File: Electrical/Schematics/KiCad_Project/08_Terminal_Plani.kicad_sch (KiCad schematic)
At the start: 0 parts

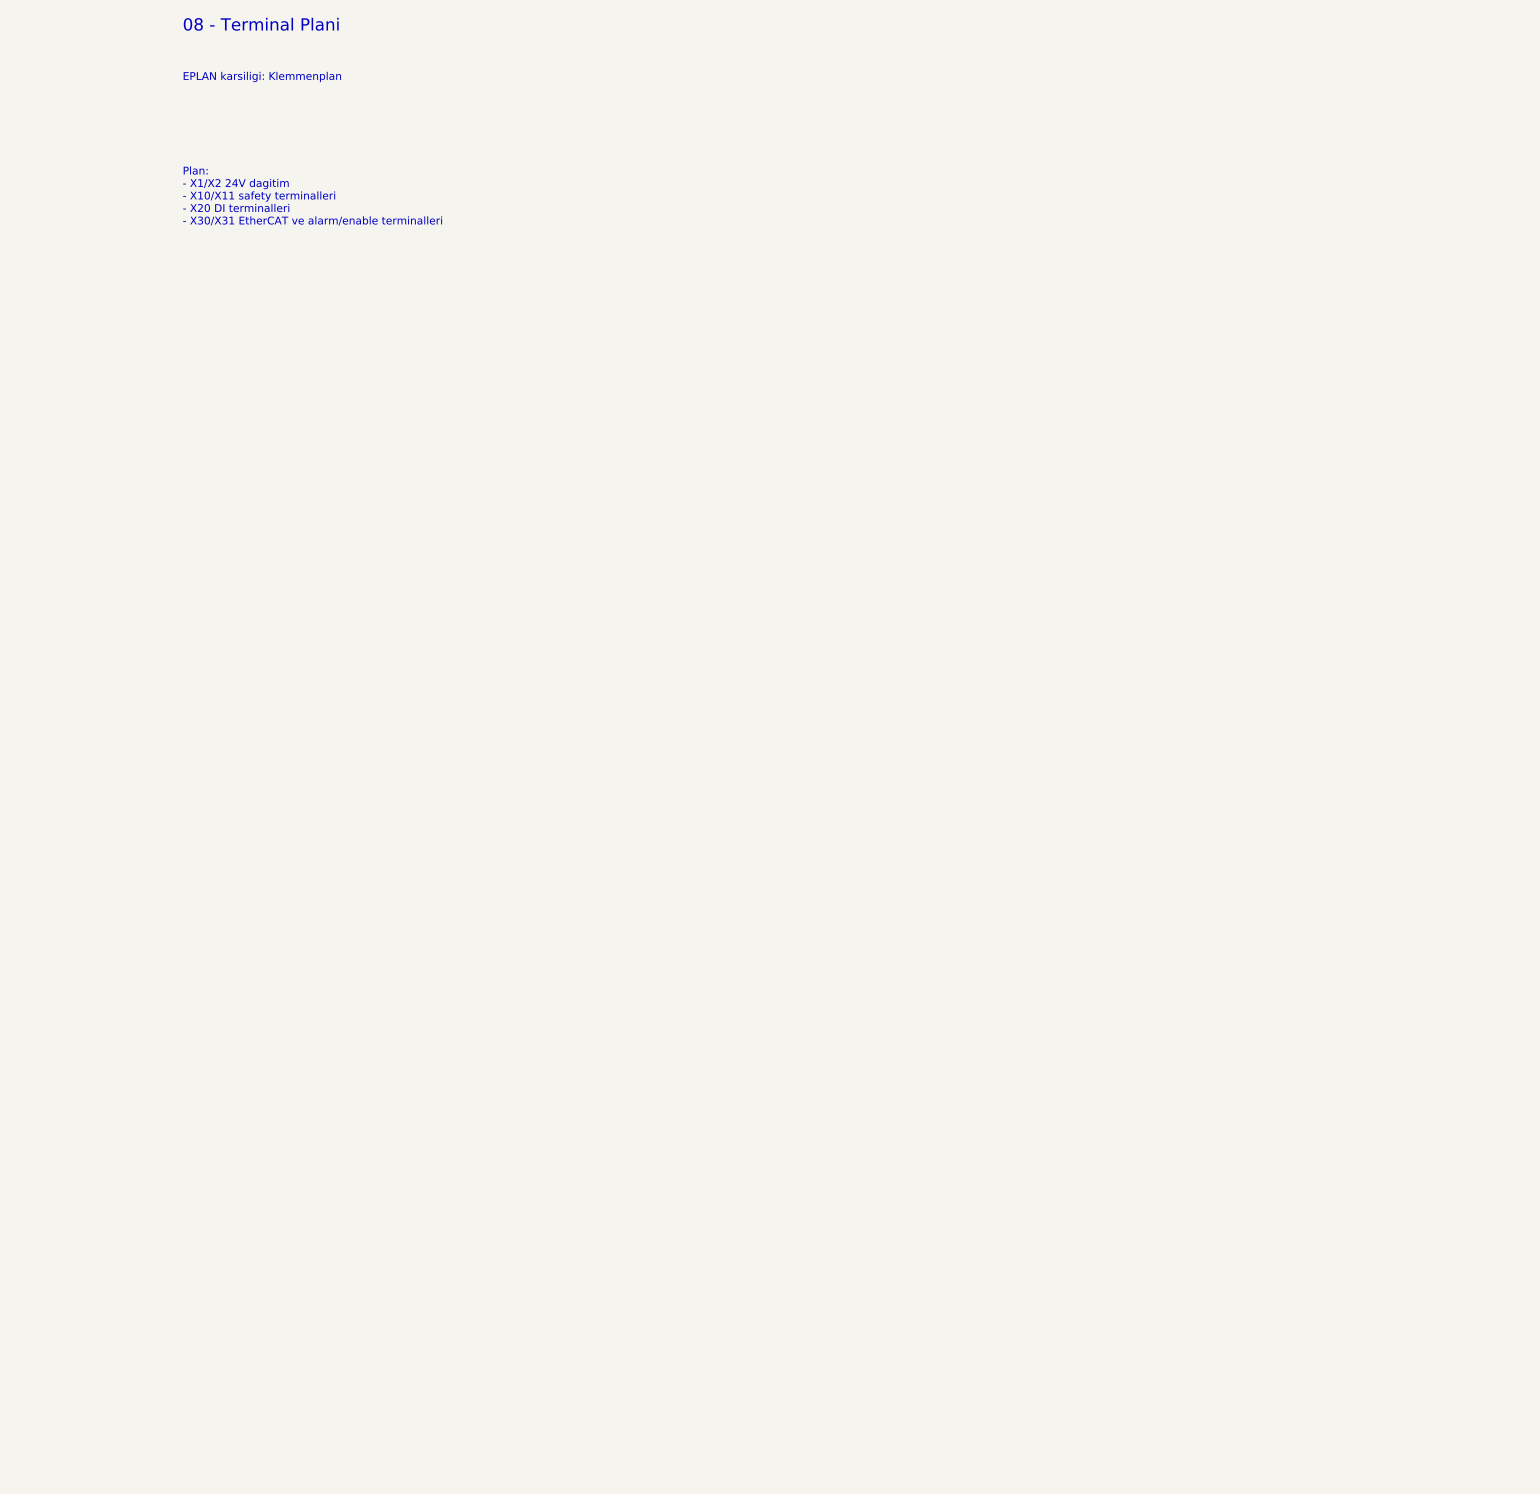
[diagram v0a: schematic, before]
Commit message: feat: update electrical schematics to rev 4.0, add technical manuals, and include project documentation and validation reports.
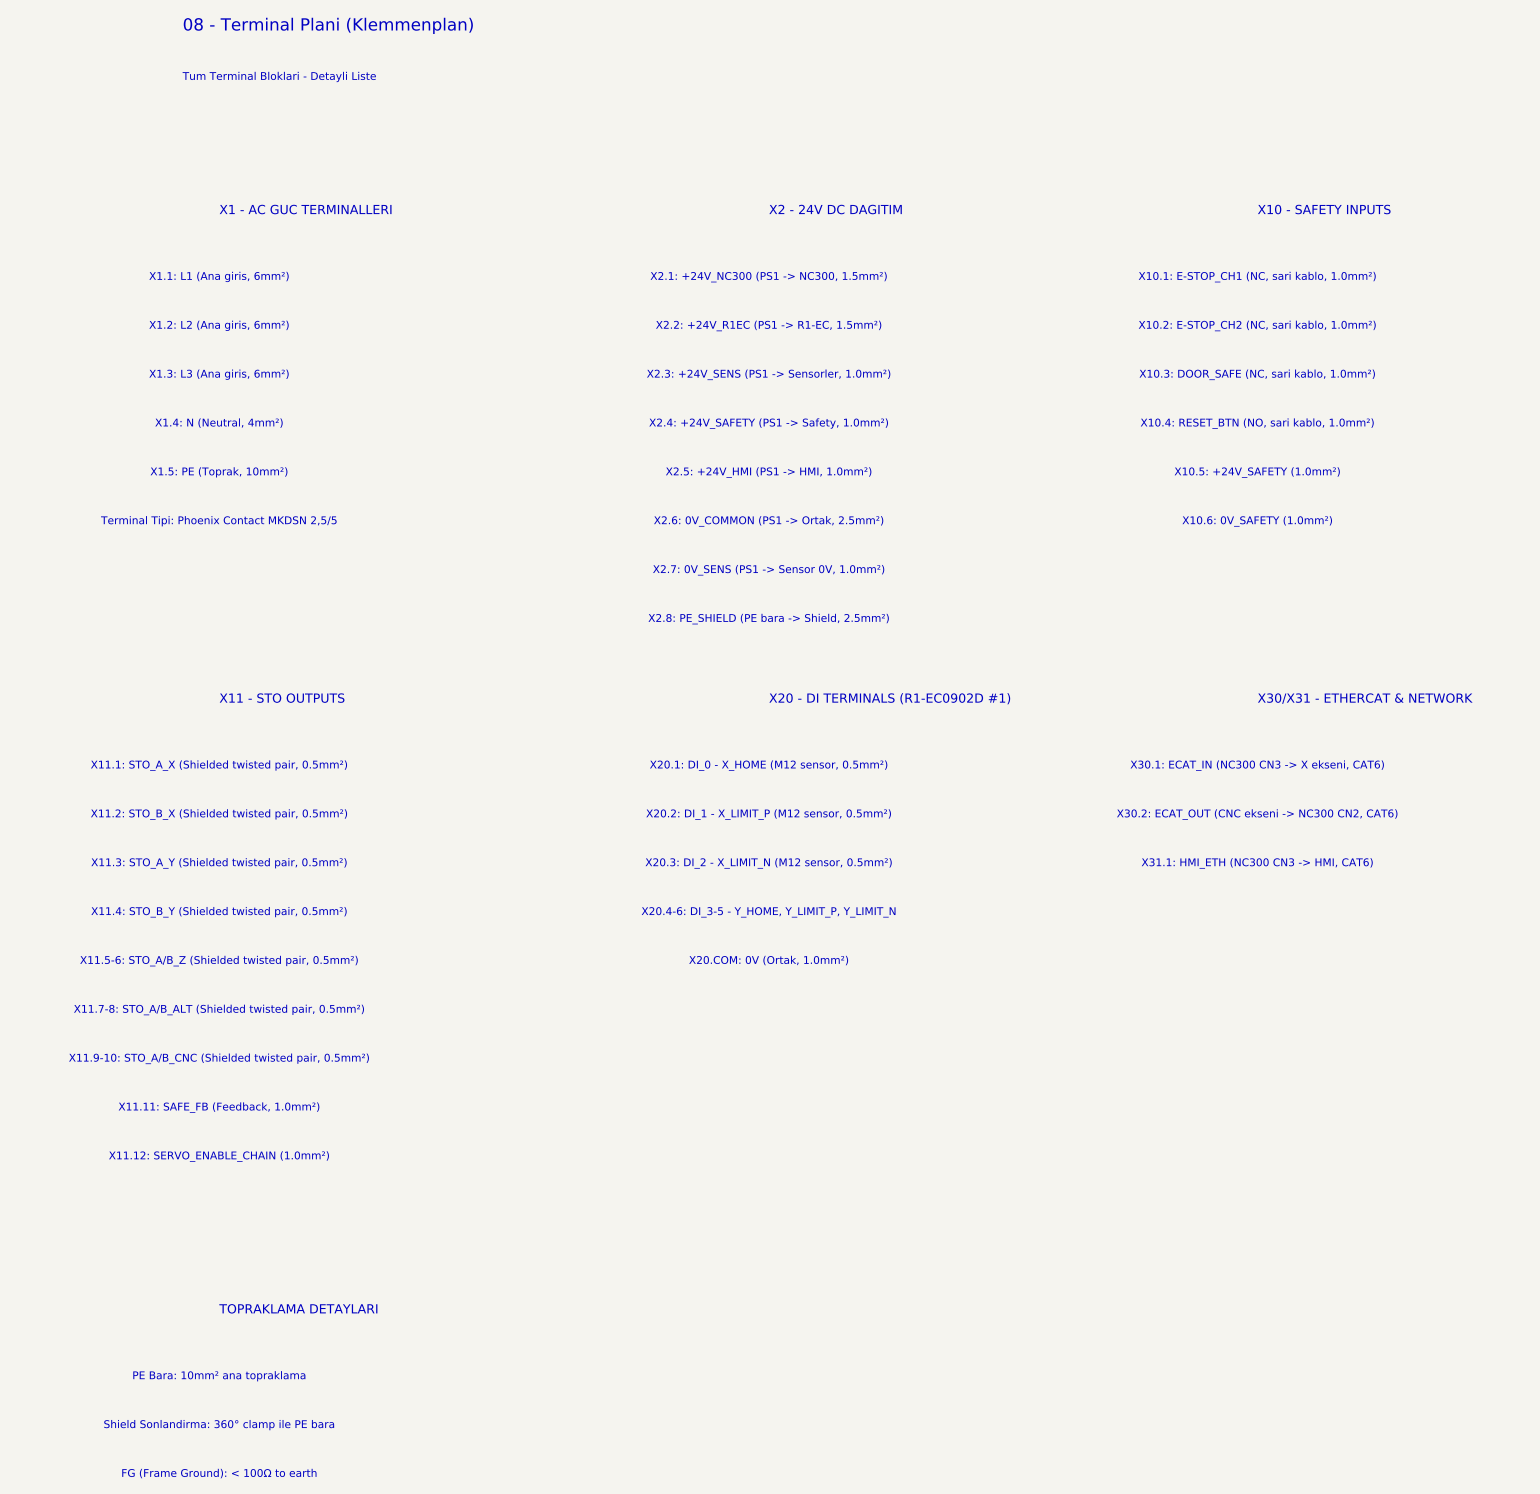
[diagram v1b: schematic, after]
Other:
- note added: "08 - Terminal Plani (Klemmenplan)"
- note added: "FG (Frame Ground): < 100Ω to earth"
- note added: "PE Bara: 10mm² ana topraklama"
- note added: "Shield Sonlandirma: 360° clamp ile PE bara"
- note added: "TOPRAKLAMA DETAYLARI"
- note added: "Terminal Tipi: Phoenix Contact MKDSN 2,5/5"
- note added: "Tum Terminal Bloklari - Detayli Liste"
- note added: "X1 - AC GUC TERMINALLERI"
- note added: "X1.1: L1 (Ana giris, 6mm²)"
- note added: "X1.2: L2 (Ana giris, 6mm²)"
- note added: "X1.3: L3 (Ana giris, 6mm²)"
- note added: "X1.4: N (Neutral, 4mm²)"
- note added: "X1.5: PE (Toprak, 10mm²)"
- note added: "X10 - SAFETY INPUTS"
- note added: "X10.1: E-STOP_CH1 (NC, sari kablo, 1.0mm²)"
- note added: "X10.2: E-STOP_CH2 (NC, sari kablo, 1.0mm²)"
- note added: "X10.3: DOOR_SAFE (NC, sari kablo, 1.0mm²)"
- note added: "X10.4: RESET_BTN (NO, sari kablo, 1.0mm²)"
- note added: "X10.5: +24V_SAFETY (1.0mm²)"
- note added: "X10.6: 0V_SAFETY (1.0mm²)"
- note added: "X11 - STO OUTPUTS"
- note added: "X11.11: SAFE_FB (Feedback, 1.0mm²)"
- note added: "X11.12: SERVO_ENABLE_CHAIN (1.0mm²)"
- note added: "X11.1: STO_A_X (Shielded twisted pair, 0.5mm²)"
- note added: "X11.2: STO_B_X (Shielded twisted pair, 0.5mm²)"
- note added: "X11.3: STO_A_Y (Shielded twisted pair, 0.5mm²)"
- note added: "X11.4: STO_B_Y (Shielded twisted pair, 0.5mm²)"
- note added: "X11.5-6: STO_A/B_Z (Shielded twisted pair, 0.5mm²)"
- note added: "X11.7-8: STO_A/B_ALT (Shielded twisted pair, 0.5mm²)"
- note added: "X11.9-10: STO_A/B_CNC (Shielded twisted pair, 0.5mm²)"
- note added: "X2 - 24V DC DAGITIM"
- note added: "X2.1: +24V_NC300 (PS1 -> NC300, 1.5mm²)"
- note added: "X2.2: +24V_R1EC (PS1 -> R1-EC, 1.5mm²)"
- note added: "X2.3: +24V_SENS (PS1 -> Sensorler, 1.0mm²)"
- note added: "X2.4: +24V_SAFETY (PS1 -> Safety, 1.0mm²)"
- note added: "X2.5: +24V_HMI (PS1 -> HMI, 1.0mm²)"
- note added: "X2.6: 0V_COMMON (PS1 -> Ortak, 2.5mm²)"
- note added: "X2.7: 0V_SENS (PS1 -> Sensor 0V, 1.0mm²)"
- note added: "X2.8: PE_SHIELD (PE bara -> Shield, 2.5mm²)"
- note added: "X20 - DI TERMINALS (R1-EC0902D #1)"
- note added: "X20.1: DI_0 - X_HOME (M12 sensor, 0.5mm²)"
- note added: "X20.2: DI_1 - X_LIMIT_P (M12 sensor, 0.5mm²)"
- note added: "X20.3: DI_2 - X_LIMIT_N (M12 sensor, 0.5mm²)"
- note added: "X20.4-6: DI_3-5 - Y_HOME, Y_LIMIT_P, Y_LIMIT_N"
- note added: "X20.COM: 0V (Ortak, 1.0mm²)"
- note added: "X30.1: ECAT_IN (NC300 CN3 -> X ekseni, CAT6)"
- note added: "X30.2: ECAT_OUT (CNC ekseni -> NC300 CN2, CAT6)"
- note added: "X30/X31 - ETHERCAT & NETWORK"
- note added: "X31.1: HMI_ETH (NC300 CN3 -> HMI, CAT6)"
- note removed: "08 - Terminal Plani"
- note removed: "EPLAN karsiligi: Klemmenplan"
- note removed: "Plan: - X1/X2 24V dagitim - X10/X11 safety terminalleri - X20 DI terminalleri - X30/X31 EtherCAT ve alarm/enable terminalleri"
- company: CNCRevizyon -> CNCRevizyon - GFB60/30RE-S
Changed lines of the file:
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@@
 	(title_block
 		(title "08 Terminal Plani")
-		(company "CNCRevizyon")
-		(rev "3.0")
-		(date "2026-04-05")
-	)
-	(text "08 - Terminal Plani" (exclude_from_sim no) (at 24 20 0)
+		(company "CNCRevizyon - GFB60/30RE-S")
+		(rev "4.0")
+		(date "2026-04-06")
+		(comment 1 "Tum terminal bloklari detayli liste")
+		(comment 2 "Kaynak: gfb_EP034-047170.pdf Sayfa 90-110 (Klemmenplan)")
+		(comment 3 "X1/X2/X10/X11/X20/X30/X31 terminalleri")
+	)
+	(text "08 - Terminal Plani (Klemmenplan)" (exclude_from_sim no) (at 24 20 0)
 		(effects (font (size 2 2)) (justify left bottom))
-	)
-	(text "EPLAN karsiligi: Klemmenplan" (exclude_from_sim no) (at 24 28 0)
+		(uuid "t08001")
+	)
+	(text "Tum Terminal Bloklari - Detayli Liste" (exclude_from_sim no) (at 24 28 0)
 		(effects (font (size 1.27 1.27)) (justify left bottom))
-	)
-	(text "Plan:\n- X1/X2 24V dagitim\n- X10/X11 safety terminalleri\n- X20 DI terminalleri\n- X30/X31 EtherCAT ve alarm/enable terminalleri" (exclude_from_sim no) (at 24 42 0)
-		(effects (font (size 1.27 1.27)) (justify left top))
+		(uuid "t08002")
+	)
+	(text "X1 - AC GUC TERMINALLERI" (exclude_from_sim no) (at 30 50 0)
+		(effects (font (size 1.5 1.5)) (justify left bottom))
+		(uuid "t08010")
+	)
+	(text "X1.1: L1 (Ana giris, 6mm²)" (exclude_from_sim no) (at 30 60 0)
+		(effects (font (size 1.27 1.27)))
+		(uuid "t08011")
+	)
+	(text "X1.2: L2 (Ana giris, 6mm²)" (exclude_from_sim no) (at 30 68 0)
+		(effects (font (size 1.27 1.27)))
+		(uuid "t08012")
+	)
+	(text "X1.3: L3 (Ana giris, 6mm²)" (exclude_from_sim no) (at 30 76 0)
+		(effects (font (size 1.27 1.27)))
+		(uuid "t08013")
+	)
+	(text "X1.4: N (Neutral, 4mm²)" (exclude_from_sim no) (at 30 84 0)
+		(effects (font (size 1.27 1.27)))
+		(uuid "t08014")
+	)
+	(text "X1.5: PE (Toprak, 10mm²)" (exclude_from_sim no) (at 30 92 0)
+		(effects (font (size 1.27 1.27)))
+		(uuid "t08015")
+	)
+	(text "Terminal Tipi: Phoenix Contact MKDSN 2,5/5" (exclude_from_sim no) (at 30 100 0)
+		(effects (font (size 1.27 1.27)))
+		(uuid "t08016")
+	)
+	(text "X2 - 24V DC DAGITIM" (exclude_from_sim no) (at 120 50 0)
+		(effects (font (size 1.5 1.5)) (justify left bottom))
+		(uuid "t08020")
+	)
+	(text "X2.1: +24V_NC300 (PS1 -> NC300, 1.5mm²)" (exclude_from_sim no) (at 120 60 0)
+		(effects (font (size 1.27 1.27)))
+		(uuid "t08021")
+	)
+	(text "X2.2: +24V_R1EC (PS1 -> R1-EC, 1.5mm²)" (exclude_from_sim no) (at 120 68 0)
+		(effects (font (size 1.27 1.27)))
+		(uuid "t08022")
+	)
+	(text "X2.3: +24V_SENS (PS1 -> Sensorler, 1.0mm²)" (exclude_from_sim no) (at 120 76 0)
+		(effects (font (size 1.27 1.27)))
+		(uuid "t08023")
+	)
+	(text "X2.4: +24V_SAFETY (PS1 -> Safety, 1.0mm²)" (exclude_from_sim no) (at 120 84 0)
+		(effects (font (size 1.27 1.27)))
+		(uuid "t08024")
+	)
+	(text "X2.5: +24V_HMI (PS1 -> HMI, 1.0mm²)" (exclude_from_sim no) (at 120 92 0)
+		(effects (font (size 1.27 1.27)))
+		(uuid "t08025")
+	)
+	(text "X2.6: 0V_COMMON (PS1 -> Ortak, 2.5mm²)" (exclude_from_sim no) (at 120 100 0)
+		(effects (font (size 1.27 1.27)))
+		(uuid "t08026")
+	)
+	(text "X2.7: 0V_SENS (PS1 -> Sensor 0V, 1.0mm²)" (exclude_from_sim no) (at 120 108 0)
+		(effects (font (size 1.27 1.27)))
+		(uuid "t08027")
+	)
+	(text "X2.8: PE_SHIELD (PE bara -> Shield, 2.5mm²)" (exclude_from_sim no) (at 120 116 0)
+		(effects (font (size 1.27 1.27)))
+		(uuid "t08028")
+	)
+	(text "X10 - SAFETY INPUTS" (exclude_from_sim no) (at 200 50 0)
+		(effects (font (size 1.5 1.5)) (justify left bottom))
+		(uuid "t08030")
+	)
+	(text "X10.1: E-STOP_CH1 (NC, sari kablo, 1.0mm²)" (exclude_from_sim no) (at 200 60 0)
+		(effects (font (size 1.27 1.27)))
+		(uuid "t08031")
+	)
+	(text "X10.2: E-STOP_CH2 (NC, sari kablo, 1.0mm²)" (exclude_from_sim no) (at 200 68 0)
+		(effects (font (size 1.27 1.27)))
+		(uuid "t08032")
+	)
+	(text "X10.3: DOOR_SAFE (NC, sari kablo, 1.0mm²)" (exclude_from_sim no) (at 200 76 0)
+		(effects (font (size 1.27 1.27)))
+		(uuid "t08033")
+	)
+	(text "X10.4: RESET_BTN (NO, sari kablo, 1.0mm²)" (exclude_from_sim no) (at 200 84 0)
+		(effects (font (size 1.27 1.27)))
+		(uuid "t08034")
+	)
+	(text "X10.5: +24V_SAFETY (1.0mm²)" (exclude_from_sim no) (at 200 92 0)
+		(effects (font (size 1.27 1.27)))
+		(uuid "t08035")
+	)
+	(text "X10.6: 0V_SAFETY (1.0mm²)" (exclude_from_sim no) (at 200 100 0)
+		(effects (font (size 1.27 1.27)))
+		(uuid "t08036")
+	)
+	(text "X11 - STO OUTPUTS" (exclude_from_sim no) (at 30 130 0)
+		(effects (font (size 1.5 1.5)) (justify left bottom))
+		(uuid "t08040")
+	)
+	(text "X11.1: STO_A_X (Shielded twisted pair, 0.5mm²)" (exclude_from_sim no) (at 30 140 0)
+		(effects (font (size 1.27 1.27)))
+		(uuid "t08041")
+	)
+	(text "X11.2: STO_B_X (Shielded twisted pair, 0.5mm²)" (exclude_from_sim no) (at 30 148 0)
+		(effects (font (size 1.27 1.27)))
+		(uuid "t08042")
+	)
+	(text "X11.3: STO_A_Y (Shielded twisted pair, 0.5mm²)" (exclude_from_sim no) (at 30 156 0)
+		(effects (font (size 1.27 1.27)))
+		(uuid "t08043")
+	)
+	(text "X11.4: STO_B_Y (Shielded twisted pair, 0.5mm²)" (exclude_from_sim no) (at 30 164 0)
+		(effects (font (size 1.27 1.27)))
+		(uuid "t08044")
+	)
+	(text "X11.5-6: STO_A/B_Z (Shielded twisted pair, 0.5mm²)" (exclude_from_sim no) (at 30 172 0)
+		(effects (font (size 1.27 1.27)))
+		(uuid "t08045")
+	)
+	(text "X11.7-8: STO_A/B_ALT (Shielded twisted pair, 0.5mm²)" (exclude_from_sim no) (at 30 180 0)
+		(effects (font (size 1.27 1.27)))
+		(uuid "t08046")
+	)
+	(text "X11.9-10: STO_A/B_CNC (Shielded twisted pair, 0.5mm²)" (exclude_from_sim no) (at 30 188 0)
+		(effects (font (size 1.27 1.27)))
+		(uuid "t08047")
+	)
+	(text "X11.11: SAFE_FB (Feedback, 1.0mm²)" (exclude_from_sim no) (at 30 196 0)
+		(effects (font (size 1.27 1.27)))
+		(uuid "t08048")
+	)
+	(text "X11.12: SERVO_ENABLE_CHAIN (1.0mm²)" (exclude_from_sim no) (at 30 204 0)
+		(effects (font (size 1.27 1.27)))
+		(uuid "t08049")
+	)
+	(text "X20 - DI TERMINALS (R1-EC0902D #1)" (exclude_from_sim no) (at 120 130 0)
+		(effects (font (size 1.5 1.5)) (justify left bottom))
+		(uuid "t08050")
+	)
+	(text "X20.1: DI_0 - X_HOME (M12 sensor, 0.5mm²)" (exclude_from_sim no) (at 120 140 0)
+		(effects (font (size 1.27 1.27)))
+		(uuid "t08051")
+	)
+	(text "X20.2: DI_1 - X_LIMIT_P (M12 sensor, 0.5mm²)" (exclude_from_sim no) (at 120 148 0)
+		(effects (font (size 1.27 1.27)))
+		(uuid "t08052")
+	)
+	(text "X20.3: DI_2 - X_LIMIT_N (M12 sensor, 0.5mm²)" (exclude_from_sim no) (at 120 156 0)
+		(effects (font (size 1.27 1.27)))
+		(uuid "t08053")
+	)
+	(text "X20.4-6: DI_3-5 - Y_HOME, Y_LIMIT_P, Y_LIMIT_N" (exclude_from_sim no) (at 120 164 0)
+		(effects (font (size 1.27 1.27)))
+		(uuid "t08054")
+	)
+	(text "X20.COM: 0V (Ortak, 1.0mm²)" (exclude_from_sim no) (at 120 172 0)
+		(effects (font (size 1.27 1.27)))
+		(uuid "t08055")
+	)
+	(text "X30/X31 - ETHERCAT & NETWORK" (exclude_from_sim no) (at 200 130 0)
+		(effects (font (size 1.5 1.5)) (justify left bottom))
+		(uuid "t08060")
+	)
+	(text "X30.1: ECAT_IN (NC300 CN3 -> X ekseni, CAT6)" (exclude_from_sim no) (at 200 140 0)
+		(effects (font (size 1.27 1.27)))
+		(uuid "t08061")
+	)
+	(text "X30.2: ECAT_OUT (CNC ekseni -> NC300 CN2, CAT6)" (exclude_from_sim no) (at 200 148 0)
+		(effects (font (size 1.27 1.27)))
+		(uuid "t08062")
+	)
+	(text "X31.1: HMI_ETH (NC300 CN3 -> HMI, CAT6)" (exclude_from_sim no) (at 200 156 0)
+		(effects (font (size 1.27 1.27)))
+		(uuid "t08063")
+	)
+	(text "TOPRAKLAMA DETAYLARI" (exclude_from_sim no) (at 30 230 0)
+		(effects (font (size 1.5 1.5)) (justify left bottom))
+		(uuid "t08070")
+	)
+	(text "PE Bara: 10mm² ana topraklama" (exclude_from_sim no) (at 30 240 0)
+		(effects (font (size 1.27 1.27)))
+		(uuid "t08071")
+	)
+	(text "Shield Sonlandirma: 360° clamp ile PE bara" (exclude_from_sim no) (at 30 248 0)
+		(effects (font (size 1.27 1.27)))
+		(uuid "t08072")
+	)
+	(text "FG (Frame Ground): < 100Ω to earth" (exclude_from_sim no) (at 30 256 0)
+		(effects (font (size 1.27 1.27)))
+		(uuid "t08073")
 	)
 	(sheet_instances
